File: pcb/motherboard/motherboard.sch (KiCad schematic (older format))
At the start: 10 parts, among them J1 BARREL_JACK, J2 USB-MINI-B, J3 HEADER-1x05, J6 HEADER-1x10, J7 HEADER-2x03, J8 HEADER-2x03, J9 HEADER-1x06

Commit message: Revised touch and front panel PCB, Added Motherboard PCB
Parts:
- removed H1, H2, H3: Hole, Conn-Wire-Pads:Hole-Screw-#2, symbol Hole
- removed J1: BARREL_JACK, Conn-Power:CUI-P1J-021-SMT, symbol BARREL_JACK
- removed J2: USB-MINI-B, Conn-IO:USB-MB_UX60SC-MB-5ST, symbol USB-MINI-B
- removed J3: HEADER-1x05, Conn-Header:HDR-M-1x05, symbol HEADER-1x05
- removed J6: HEADER-1x10, Conn-Header:HDR-M-1x10, symbol HEADER-1x10
- removed J8: HEADER-2x03, Conn-Header:HDR-M-2x03, symbol HEADER-2x03
- removed J9: HEADER-1x06, Conn-Header:DF3A-6P-2DSA, symbol HEADER-1x06
- added C10, C22, C23, C24, C25, C26: 100nF, smt:C-0603, symbol passive:CAP
- added C12: 22pF, smt:C-0603, symbol passive:CAP
- added C13: 1uF, smt:C-0805, symbol passive:CAP
- added C7, C8: 20pF, smt:C-0603, symbol passive:CAP
- added D1: 1N4148, smt:SOD-323, symbol passive:DIODE
- added H1, H2, H3: Hole, conn-wire-pads:Hole-Screw-#4, symbol connectors:Hole
- added H4, H5: HEADER-1x01, conn-wire-pads:SolderPad-100x500, symbol connectors:HEADER-1x01
- added H6: HEADER-1x01, conn-wire-pads:SolderPad-100x300, symbol connectors:HEADER-1x01
- added J1: -, conn-power:CUI-P1J-021-SMT, symbol connectors:BARREL_JACK
- added J10: PSU, conn-header:HDR-M-2x03, symbol connectors:HEADER-2x03
- added J11, J12: PSU-GND, conn-header:HDR-M-1x01, symbol connectors:HEADER-1x01
- added J14: EXT, conn-wire-pads:WP-40mil-1x05, symbol connectors:HEADER-1x05
- added J15: EXT-PW, conn-wire-pads:WP-50mil-1x02, symbol connectors:HEADER-1x02
- added J16: EXT-I2C, conn-wire-pads:WP-50mil-1x02, symbol connectors:HEADER-1x02
- added J6: PSU-SIG, conn-header:HDR-M-1x02, symbol connectors:HEADER-1x02
- added J8: FRONT PANEL, conn-wire-pads:WP-50mil-1x06, symbol connectors:HEADER-1x06
- added R19: 300, smt:C-0603, symbol passive:RESISTOR
- added R20, R21: 10k, smt:C-0603, symbol passive:RESISTOR
- added R6, R9: 10k, smt:R-0603, symbol passive:RESISTOR
- added R8: 1M, smt:R-0603, symbol passive:RESISTOR
- added SW1: RESET, switches:B3F-10XX, symbol switches:MOM-SPST
- added U1: ATMEGA2560-16AU, smt-qfp:QFP-14-100, symbol ic-cpu:ATMEGA2560-16AU
- added Y2: 16.00 MHz, crystals:HC49USX, symbol passive:CRYSTAL
- J7: value HEADER-2x03 -> ICSP; footprint Conn-Header:HDR-M-2x03 -> conn-header:HDR-M-2x03; symbol HEADER-2x03 -> connectors:HEADER-2x03; Part - -> CES-103-01-T-D
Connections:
- net labels added: +5V, ALRM_SW, ALS_INT, A_SHDN, CCS, CFG\~RST, CRST, DREQ, KCHG, LOW_BATT, MISO, MOSI, OLRST, ON_BATT, P42, P43, P44, P45, P46, PIX_CLK, PIX_LAMP, PIX_SHDN, RESET, RTC_INT, RXD0, SCK, SCL, SDA, SDCS, SD_DET, SUP_+5V, TXD0, VIN, WCS, WEN, WIRQ, WRST, WWAKE, XDCS
- net labels removed: SUP_GND
- wire segments 7 -> 192
- no-connect marks 1 -> 54
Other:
- note added: "ICSP"
- note added: "P0"
- note added: "P1"
- note added: "P10"
- note added: "P11"
- note added: "P12"
- note added: "P13"
- note added: "P16"
- note added: "P18"
- note added: "P19"
- note added: "P2"
- note added: "P20"
- note added: "P21"
- note added: "P25"
- note added: "P26"
- note added: "P27"
- note added: "P28"
- note added: "P29"
- note added: "P3"
- note added: "P30"
- note added: "P33"
- note added: "P35"
- note added: "P37"
- note added: "P4"
- note added: "P5"
- note added: "P50"
- note added: "P51"
- note added: "P52"
- note added: "P6"
- note added: "P8"
- note added: "P9"
- note added: "PSU"
- note added: "RESET / FACTORY CONFIG"

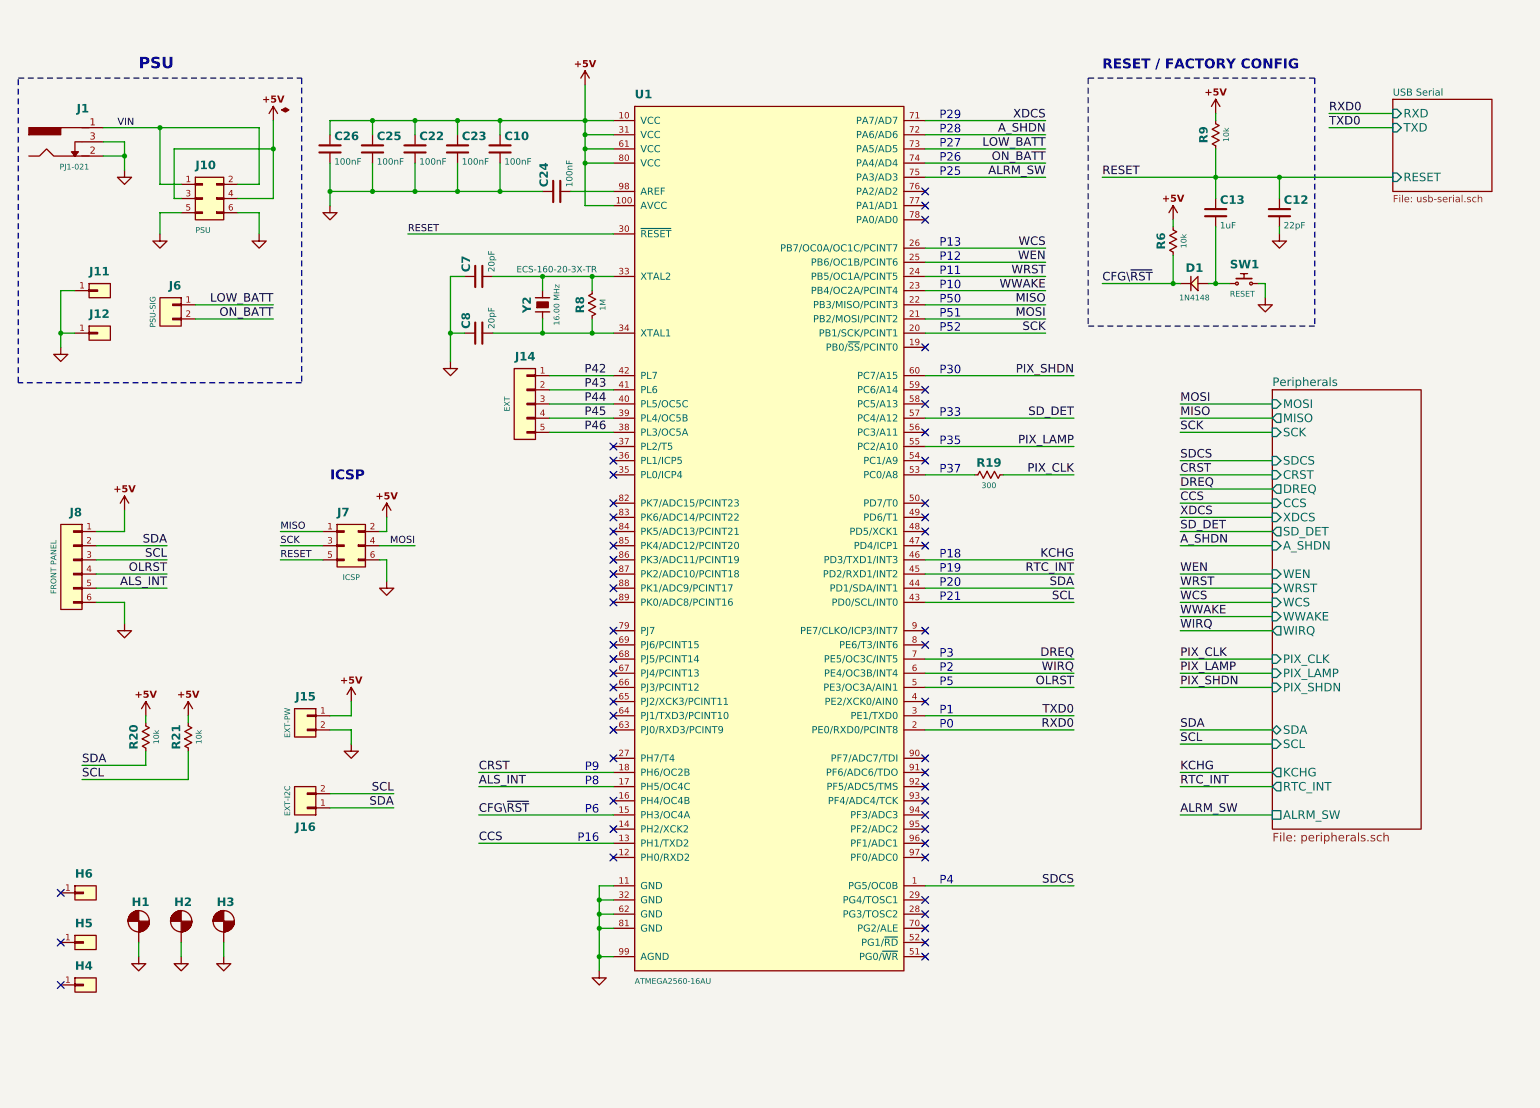
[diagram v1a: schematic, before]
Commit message: Adjusted page size for motherboard schematic
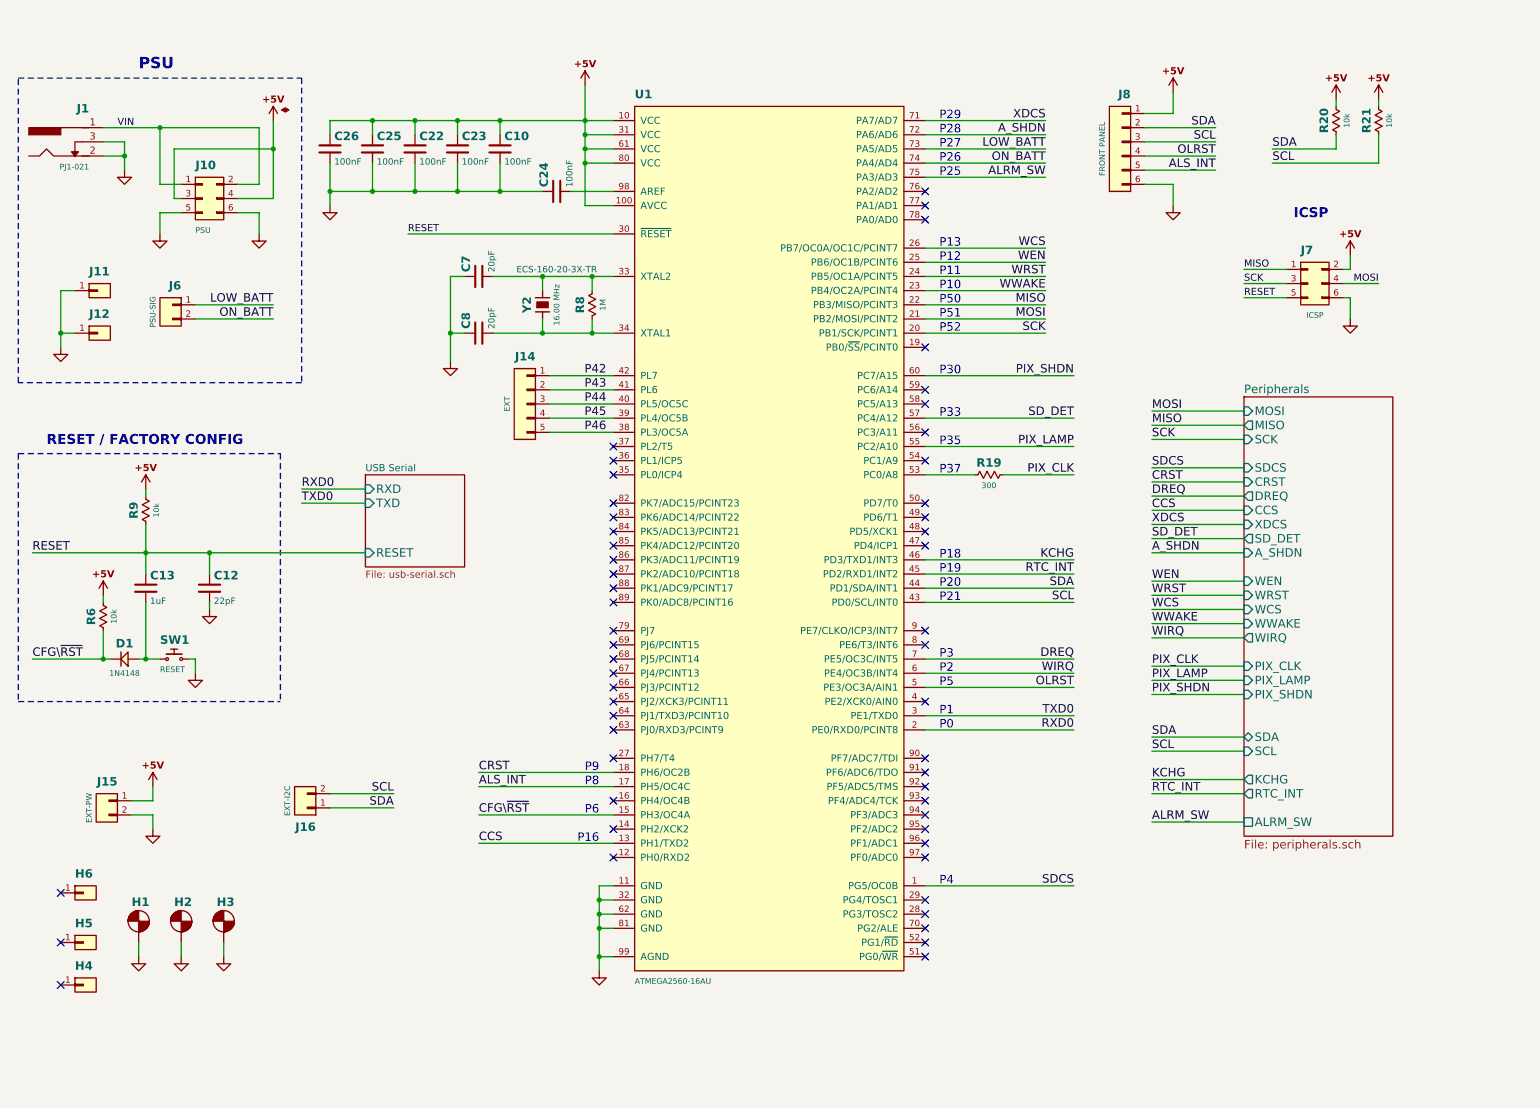
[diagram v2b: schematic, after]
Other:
- moved on the sheet: C12, C13, D1, J15, J7, J8, R20, R21, R6, R9, SW1

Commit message: Updated PCB design
+ Completed daughterboard PCB layout.
* Corrected soldermask clerance on front panel pcb.
- Removed input resistor on DIN for RGB lamp board.
* Modified PCB layout for PSU board.
* Updated gerber files.
* Updated schematics pdf, BOM.
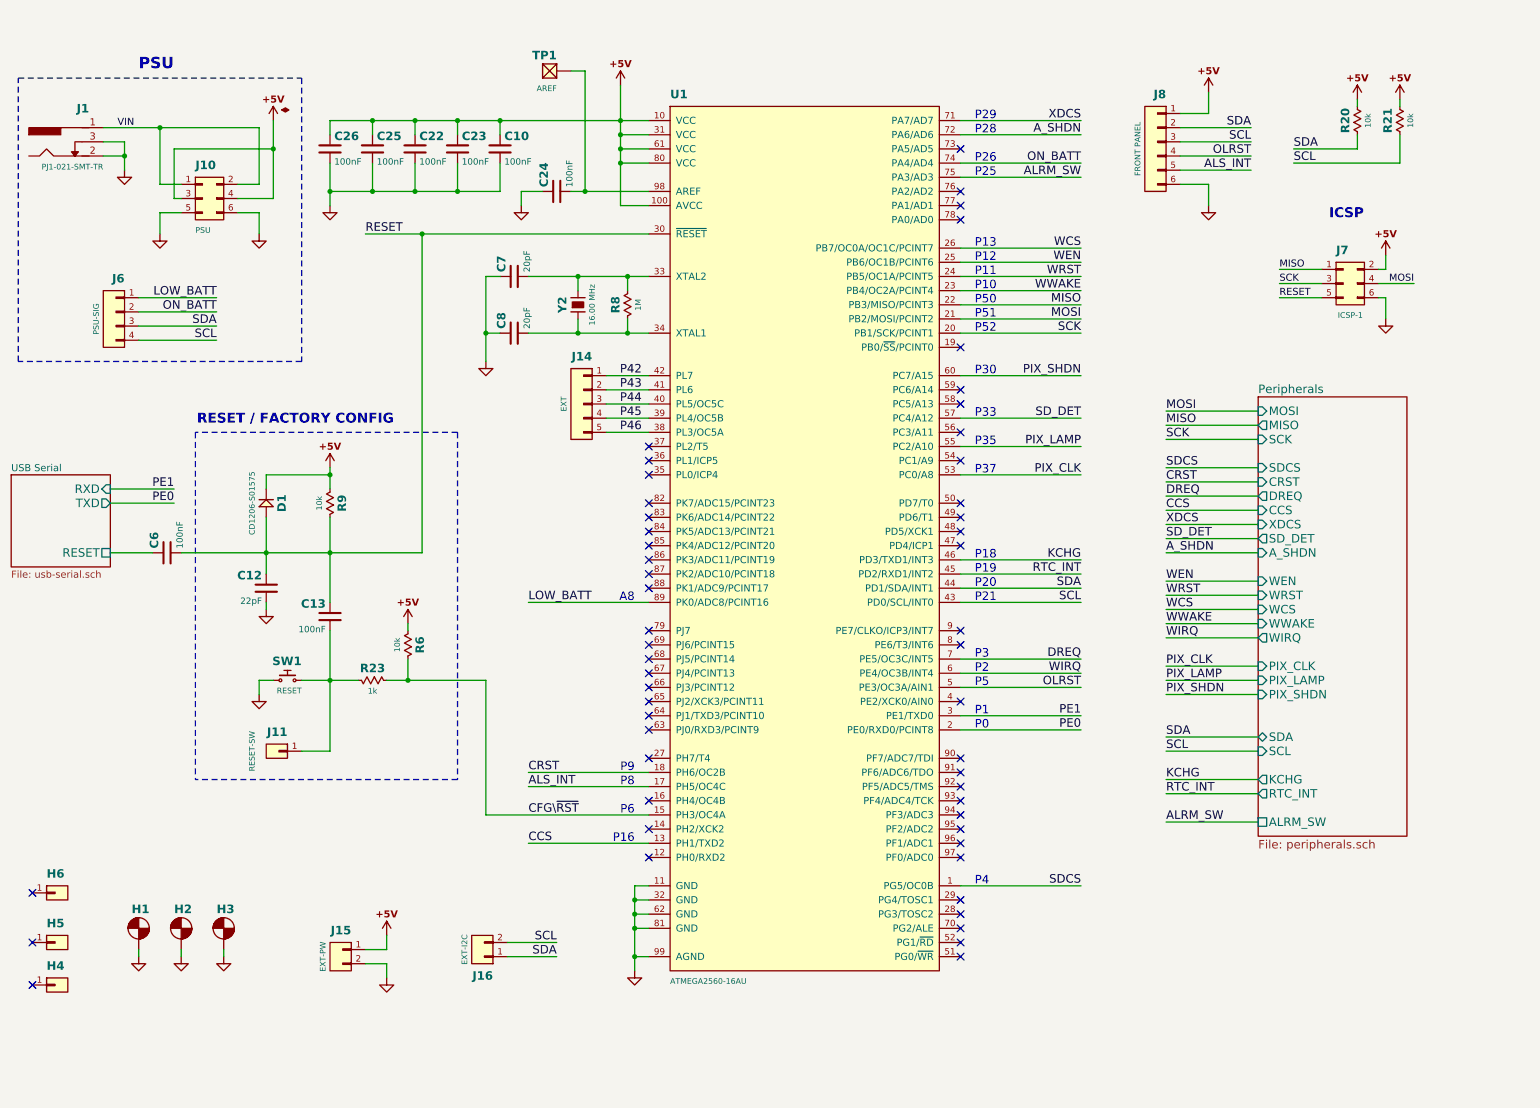
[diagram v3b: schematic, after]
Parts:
- removed J12: PSU-GND, conn-header:HDR-M-1x01, symbol connectors:HEADER-1x01
- removed J6: PSU-SIG, conn-header:HDR-M-1x02, symbol connectors:HEADER-1x02
- removed R19: 300, smt:C-0603, symbol passive:RESISTOR
- added C6: 100nF, smt:C-0603, symbol passive:CAP
- added J6: PSU-SIG, conn-header:HDR-M-1x04, symbol connectors:HEADER-1x04
- added R23: 1k, smt:R-0603, symbol passive:RESISTOR
- added TP1: AREF, conn-wire-pads:TEST-POINT-50, symbol connectors:TEST-POINT
- C13: value 1uF -> 100nF; footprint smt:C-0805 -> smt:C-0603
- D1: value 1N4148 -> CD1206-S01575; footprint smt:SOD-323 -> smt:D-1206; Part - -> CD1206-S01575
- J1: Part PJ1-021 -> PJ1-021-SMT-TR
- J10: Part DW-03-08-T-D-300 -> BCS-103-L-D-TE
- J11: value PSU-GND -> RESET-SW; footprint conn-header:HDR-M-1x01 -> conn-wire-pads:WP-50mil-1x01; Family Connector -> Virtual; Part DW-01-08-T-S-300 -> -
- J7: value ICSP -> ICSP-1
- Y2: footprint crystals:HC49USX -> crystals:smt-CSM-3X-7x4mm
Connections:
- net +5V: now also D1.K
- net CFG\~RST: now also R23.1; no longer D1.K
- net GND: no longer J11.1 (P1)
- net LOW_BATT: now also U1.89 (PK0/ADC8/PCINT16), J6.1 (P1); no longer U1.73 (PA5/AD5)
- net ON_BATT: now also J6.2 (P2)
- net PIX_CLK: now also U1.53 (PC0/A8)
- net RESET: now also D1.A, C6.1
- net SCL: now also J6.4 (P4)
- net SDA: now also J6.3 (P3)
- net at C24.1, U1.98 (AREF): now also TP1.1 (P1)
- net at C13.1, SW1.1: now also J11.1 (P1), R23.2; no longer D1.A
- net RXD0 renamed PE0
- net TXD0 renamed PE1
- new net USB Serial/RESET: C6.2
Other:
- note added: "A8"
- note removed: "P27"
- moved on the sheet: C12, C13, C7, C8, H1, H2, H3, H4, H5, H6, J14, J15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

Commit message: Changed cap C13 from 100nF to 1uF
* Use 1uF on C13 to generate a longer reset pulse when pressing the cfg/reset button.
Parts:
- C13: value 100nF -> 1uF
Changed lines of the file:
@@
 P 2800 4750
 F 0 "C13" H 2830 4840 60  0000 L CNB
-F 1 "100nF" H 2830 4660 45  0000 L CNN
+F 1 "1uF" H 2830 4660 45  0000 L CNN
 F 2 "smt:C-0603" H 2835 4595 40  0001 L CNN
 F 3 "" H 2800 4850 60  0001 C CNN
